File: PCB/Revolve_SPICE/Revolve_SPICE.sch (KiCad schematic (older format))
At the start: 8 parts, among them Q3 Q_PMOS_DGS, Q6 Q_NMOS_DGS, Q7 Q_NMOS_DGS

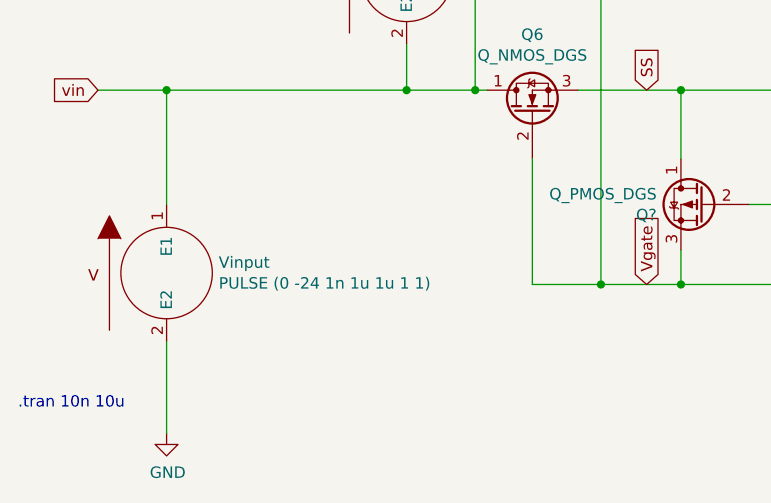
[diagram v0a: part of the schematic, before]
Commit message: Added files needed for Umikaze.
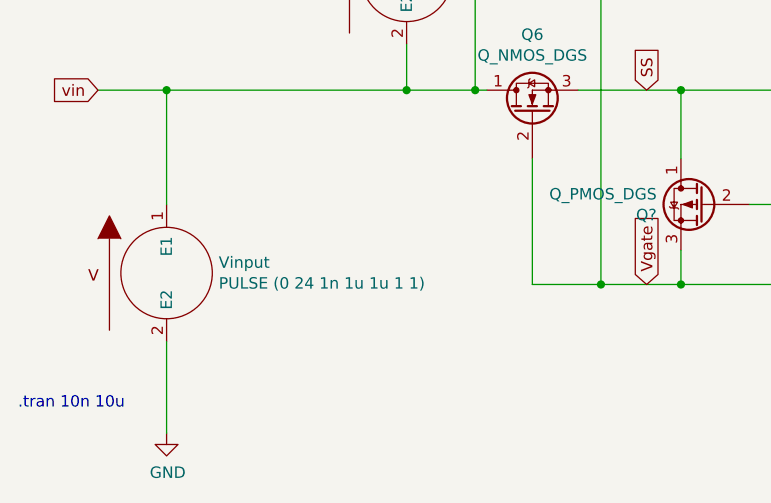
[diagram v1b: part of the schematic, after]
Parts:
- Vinput: value PULSE (0 -24 1n 1u 1u 1 1) -> PULSE (0 24 1n 1u 1u 1 1)
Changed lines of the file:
@@
 Comment4 ""
 $EndDescr
-$Comp
-L pspice:VSOURCE Vinput
-U 1 1 5D599E1E
-P 1900 3950
-F 0 "Vinput" H 2128 3996 50  0000 L CNN
-F 1 "PULSE (0 -24 1n 1u 1u 1 1)" H 2128 3905 50  0000 L CNN
-F 2 "" H 1900 3950 50  0001 C CNN
-F 3 "~" H 1900 3950 50  0001 C CNN
-F 4 "V" H 1900 3950 50  0001 C CNN "Spice_Primitive"
-F 5 "Y" H 1900 3950 50  0001 C CNN "Spice_Netlist_Enabled"
-	1    1900 3950
-	1    0    0    -1
-$EndComp
 Wire Wire Line
 	1600 3150 1900 3150
@@
 Text GLabel 6750 3150 2    50   Input ~ 0
 vout
-Text Notes 1250 4550 0    50   ~ 0
-.tran 10n 10u
-$Comp
-L Device:R R1
-U 1 1 5E4EB923
-P 6150 3600
-F 0 "R1" H 6220 3646 50  0000 L CNN
-F 1 "1K" H 6220 3555 50  0000 L CNN
-F 2 "" V 6080 3600 50  0001 C CNN
-F 3 "~" H 6150 3600 50  0001 C CNN
-	1    6150 3600
-	1    0    0    -1
-$EndComp
 Wire Wire Line
 	6150 3150 6150 3450
@@
 	2950 2350 2950 2100
 Wire Wire Line
+	2950 2100 3800 2100
+$Comp
+L Device:Q_NMOS_DGS Q6
+U 1 1 5DB5B5C4
+P 3500 3250
+F 0 "Q6" V 3843 3250 50  0000 C CNN
+F 1 "Q_NMOS_DGS" V 3752 3250 50  0000 C CNN
+F 2 "" H 3700 3350 50  0001 C CNN
+F 3 "~" H 3500 3250 50  0001 C CNN
+F 4 "X" H 3500 3250 50  0001 C CNN "Spice_Primitive"
+F 5 "BSC020N03LS_L0" H 3500 3250 50  0001 C CNN "Spice_Model"
+F 6 "Y" H 3500 3250 50  0001 C CNN "Spice_Netlist_Enabled"
+F 7 "Infineon-SimulationModel_OptiMOS_PowerMOSFET_PSpice_30V_N-Channel-SM-v01_00-EN/03_OptiMOS3/OptiMOS3_30V.lib" H 3500 3250 50  0001 C CNN "Spice_Lib_File"
+	1    3500 3250
+	0    -1   -1   0
+$EndComp
+$Comp
+L Device:Q_NMOS_DGS Q7
+U 1 1 5DB63888
+P 4900 3250
+F 0 "Q7" V 5243 3250 50  0000 C CNN
+F 1 "Q_NMOS_DGS" V 5152 3250 50  0000 C CNN
+F 2 "" H 5100 3350 50  0001 C CNN
+F 3 "~" H 4900 3250 50  0001 C CNN
+F 4 "X" H 4900 3250 50  0001 C CNN "Spice_Primitive"
+F 5 "BSC020N03LS_L0" H 4900 3250 50  0001 C CNN "Spice_Model"
+F 6 "Y" H 4900 3250 50  0001 C CNN "Spice_Netlist_Enabled"
+F 7 "Infineon-SimulationModel_OptiMOS_PowerMOSFET_PSpice_30V_N-Channel-SM-v01_00-EN/03_OptiMOS3/OptiMOS3_30V.lib" H 4900 3250 50  0001 C CNN "Spice_Lib_File"
+	1    4900 3250
+	0    1    -1   0
+$EndComp
+$Comp
+L Device:Q_PMOS_DGS Q?
+U 1 1 5EB08D35
+P 4250 3650
+F 0 "Q?" H 4456 3604 50  0000 L CNN
+F 1 "Q_PMOS_DGS" H 4456 3695 50  0000 L CNN
+F 2 "" H 4450 3750 50  0001 C CNN
+F 3 "~" H 4250 3650 50  0001 C CNN
+F 4 "X" H 4250 3650 50  0001 C CNN "Spice_Primitive"
+F 5 "SiSS27DN" H 4250 3650 50  0001 C CNN "Spice_Model"
+F 6 "Y" H 4250 3650 50  0001 C CNN "Spice_Netlist_Enabled"
+F 7 "siss27dn/SiSS27DN_PS Rev A.LIB" H 4250 3650 50  0001 C CNN "Spice_Lib_File"
+	1    4250 3650
+	-1   0    0    -1
+$EndComp
+$Comp
+L pspice:VSOURCE Vct2
+U 1 1 5EB1B060
+P 5450 4200
+F 0 "Vct2" H 5678 4246 50  0000 L CNN
+F 1 "PULSE (0 24 5u 1u 1u 1 1)" H 5678 4155 50  0000 L CNN
+F 2 "" H 5450 4200 50  0001 C CNN
+F 3 "~" H 5450 4200 50  0001 C CNN
+F 4 "V" H 5450 4200 50  0001 C CNN "Spice_Primitive"
+F 5 "Y" H 5450 4200 50  0001 C CNN "Spice_Netlist_Enabled"
+	1    5450 4200
+	1    0    0    -1
+$EndComp
+$Comp
+L power:GND #PWR?
+U 1 1 5EB240A1
+P 5450 4650
+F 0 "#PWR?" H 5450 4400 50  0001 C CNN
+F 1 "GND" H 5455 4477 50  0000 C CNN
+F 2 "" H 5450 4650 50  0001 C CNN
+F 3 "" H 5450 4650 50  0001 C CNN
+	1    5450 4650
+	1    0    0    -1
+$EndComp
+Wire Wire Line
+	5450 4500 5450 4650
+Wire Wire Line
+	5450 3900 5450 3650
+Wire Wire Line
+	5450 3650 4450 3650
+Text GLabel 5450 3650 2    50   Input ~ 0
+src
+Wire Wire Line
+	4150 4000 4900 4000
+Connection ~ 4150 4000
+Wire Wire Line
+	4150 3850 4150 4000
+Wire Wire Line
+	4150 3150 4700 3150
+Wire Wire Line
+	3700 3150 4150 3150
+Connection ~ 4150 3150
+Wire Wire Line
+	4150 3150 4150 3450
+Wire Wire Line
+	6150 3750 6150 4650
+Wire Wire Line
+	3800 4000 4150 4000
+Wire Wire Line
+	3500 4000 3800 4000
+Connection ~ 3800 4000
+$Comp
+L Device:R R1
+U 1 1 5E4EB923
+P 6150 3600
+F 0 "R1" H 6220 3646 50  0000 L CNN
+F 1 "1K" H 6220 3555 50  0000 L CNN
+F 2 "" V 6080 3600 50  0001 C CNN
+F 3 "~" H 6150 3600 50  0001 C CNN
+	1    6150 3600
+	1    0    0    -1
+$EndComp
+$Comp
+L pspice:VSOURCE Vinput
+U 1 1 5D599E1E
+P 1900 3950
+F 0 "Vinput" H 2128 3996 50  0000 L CNN
+F 1 "PULSE (0 24 1n 1u 1u 1 1)" H 2128 3905 50  0000 L CNN
+F 2 "" H 1900 3950 50  0001 C CNN
+F 3 "~" H 1900 3950 50  0001 C CNN
+F 4 "V" H 1900 3950 50  0001 C CNN "Spice_Primitive"
+F 5 "Y" H 1900 3950 50  0001 C CNN "Spice_Netlist_Enabled"
+	1    1900 3950
+	1    0    0    -1
+$EndComp
+Text Notes 1250 4550 0    50   ~ 0
+.tran 10n 10u
+Wire Wire Line
+	3800 2600 3800 4000
+Wire Wire Line
 	3800 2100 3800 2200
-Wire Wire Line
-	3500 2400 3250 2400
-Wire Wire Line
-	2950 3150 3250 3150
 $Comp
 L Device:Q_PMOS_DGS Q3
@@
 $EndComp
 Wire Wire Line
-	2950 2100 3800 2100
+	3500 2400 3250 2400
+Wire Wire Line
+	3250 3150 3300 3150
+Wire Wire Line
+	2950 3150 3250 3150
+Connection ~ 3250 3150
 Wire Wire Line
 	3250 2400 3250 3150
-Connection ~ 3250 3150
-Wire Wire Line
-	3250 3150 3300 3150
-Wire Wire Line
-	3500 4000 3800 4000
-Connection ~ 3800 4000
-$Comp
-L Device:Q_NMOS_DGS Q6
-U 1 1 5DB5B5C4
-P 3500 3250
-F 0 "Q6" V 3843 3250 50  0000 C CNN
-F 1 "Q_NMOS_DGS" V 3752 3250 50  0000 C CNN
-F 2 "" H 3700 3350 50  0001 C CNN
-F 3 "~" H 3500 3250 50  0001 C CNN
-F 4 "X" H 3500 3250 50  0001 C CNN "Spice_Primitive"
-F 5 "BSC020N03LS_L0" H 3500 3250 50  0001 C CNN "Spice_Model"
-F 6 "Y" H 3500 3250 50  0001 C CNN "Spice_Netlist_Enabled"
-F 7 "Infineon-SimulationModel_OptiMOS_PowerMOSFET_PSpice_30V_N-Channel-SM-v01_00-EN/03_OptiMOS3/OptiMOS3_30V.lib" H 3500 3250 50  0001 C CNN "Spice_Lib_File"
-	1    3500 3250
-	0    -1   -1   0
-$EndComp
-$Comp
-L Device:Q_NMOS_DGS Q7
-U 1 1 5DB63888
-P 4900 3250
-F 0 "Q7" V 5243 3250 50  0000 C CNN
-F 1 "Q_NMOS_DGS" V 5152 3250 50  0000 C CNN
-F 2 "" H 5100 3350 50  0001 C CNN
-F 3 "~" H 4900 3250 50  0001 C CNN
-F 4 "X" H 4900 3250 50  0001 C CNN "Spice_Primitive"
-F 5 "BSC020N03LS_L0" H 4900 3250 50  0001 C CNN "Spice_Model"
-F 6 "Y" H 4900 3250 50  0001 C CNN "Spice_Netlist_Enabled"
-F 7 "Infineon-SimulationModel_OptiMOS_PowerMOSFET_PSpice_30V_N-Channel-SM-v01_00-EN/03_OptiMOS3/OptiMOS3_30V.lib" H 4900 3250 50  0001 C CNN "Spice_Lib_File"
-	1    4900 3250
-	0    1    -1   0
-$EndComp
-$Comp
-L Device:Q_PMOS_DGS Q?
-U 1 1 5EB08D35
-P 4250 3650
-F 0 "Q?" H 4456 3604 50  0000 L CNN
-F 1 "Q_PMOS_DGS" H 4456 3695 50  0000 L CNN
-F 2 "" H 4450 3750 50  0001 C CNN
-F 3 "~" H 4250 3650 50  0001 C CNN
-F 4 "X" H 4250 3650 50  0001 C CNN "Spice_Primitive"
-F 5 "SiSS27DN" H 4250 3650 50  0001 C CNN "Spice_Model"
-F 6 "Y" H 4250 3650 50  0001 C CNN "Spice_Netlist_Enabled"
-F 7 "siss27dn/SiSS27DN_PS Rev A.LIB" H 4250 3650 50  0001 C CNN "Spice_Lib_File"
-	1    4250 3650
-	-1   0    0    -1
-$EndComp
-$Comp
-L pspice:VSOURCE Vct2
-U 1 1 5EB1B060
-P 5450 4200
-F 0 "Vct2" H 5678 4246 50  0000 L CNN
-F 1 "PULSE (0 24 5u 1u 1u 1 1)" H 5678 4155 50  0000 L CNN
-F 2 "" H 5450 4200 50  0001 C CNN
-F 3 "~" H 5450 4200 50  0001 C CNN
-F 4 "V" H 5450 4200 50  0001 C CNN "Spice_Primitive"
-F 5 "Y" H 5450 4200 50  0001 C CNN "Spice_Netlist_Enabled"
-	1    5450 4200
-	1    0    0    -1
-$EndComp
-$Comp
-L power:GND #PWR?
-U 1 1 5EB240A1
-P 5450 4650
-F 0 "#PWR?" H 5450 4400 50  0001 C CNN
-F 1 "GND" H 5455 4477 50  0000 C CNN
-F 2 "" H 5450 4650 50  0001 C CNN
-F 3 "" H 5450 4650 50  0001 C CNN
-	1    5450 4650
-	1    0    0    -1
-$EndComp
-Wire Wire Line
-	5450 4500 5450 4650
-Wire Wire Line
-	5450 3900 5450 3650
-Wire Wire Line
-	5450 3650 4450 3650
-Text GLabel 5450 3650 2    50   Input ~ 0
-src
-Wire Wire Line
-	4150 4000 4900 4000
-Connection ~ 4150 4000
-Wire Wire Line
-	4150 3850 4150 4000
-Wire Wire Line
-	4150 3150 4700 3150
-Wire Wire Line
-	3700 3150 4150 3150
-Connection ~ 4150 3150
-Wire Wire Line
-	4150 3150 4150 3450
-Wire Wire Line
-	3800 2600 3800 4000
-Wire Wire Line
-	3800 4000 4150 4000
-Wire Wire Line
-	6150 3750 6150 4650
 $EndSCHEMATC
